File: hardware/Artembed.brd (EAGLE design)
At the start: 79.4 x 31.8 mm, 108 parts, among them J3 CORTEX_JTAG_DEBUG_MINIMUM_PTH, J4 CORTEX_JTAG_DEBUG_PTH_NS, J7 CAMERA-HIMAX, U1 DAPLINK_KL26Z, U2 16MHz, U3 ARTEMIS_MODULESMD, U4 1.8V, U5 LIS2DH12, Y1 32.768kHz

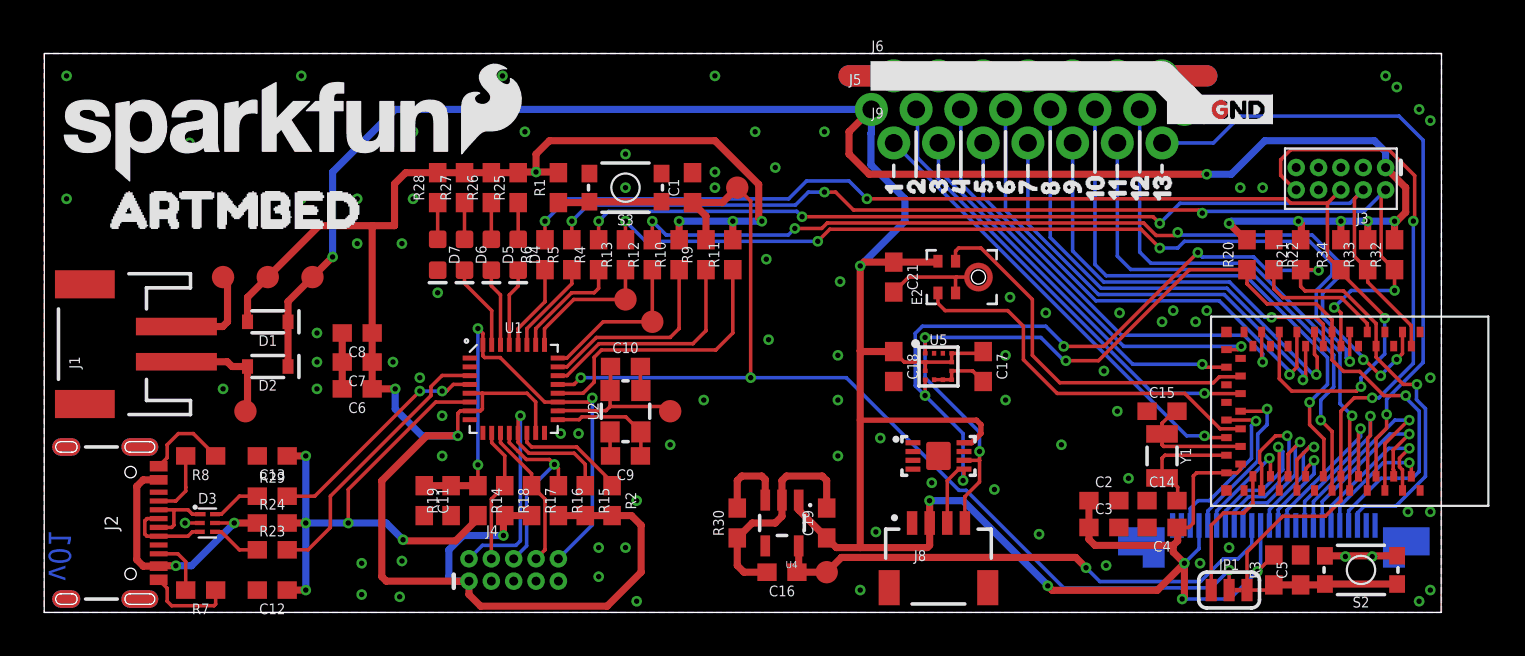
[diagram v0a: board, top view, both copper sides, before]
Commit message: Update XTAL from Eli
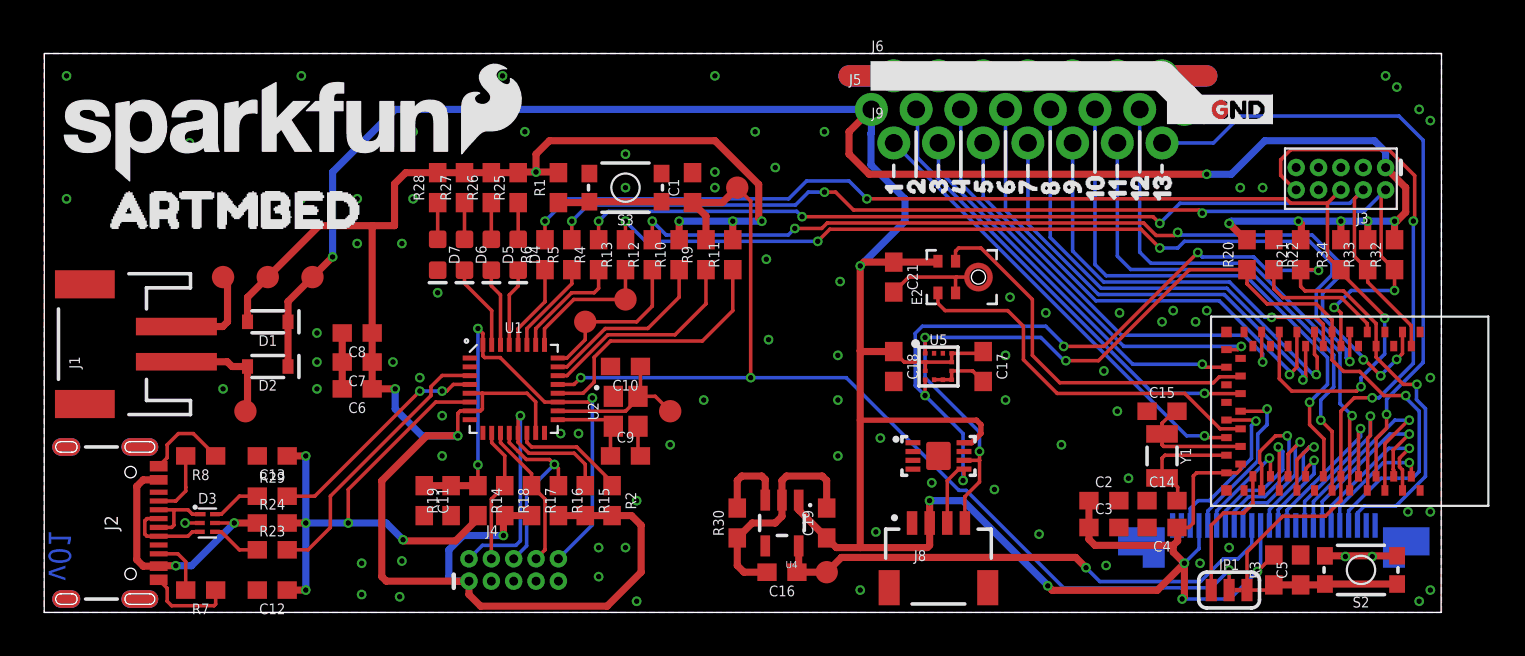
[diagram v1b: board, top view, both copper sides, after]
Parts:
- U2: device SparkFun-Clocks:CRYSTAL-SMD-3.2X2.5MM -> SparkFun-Clocks:CRYSTAL-SMD-2X2.5MM
- moved TP3 3.81 mm to (30.7, 16.5)
- turned C10 to 180 degrees
- turned C9 to 0 degrees
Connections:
- net GND: now also U2.P2, U2.P4; no longer U2.2, U2.4
- net N$13: now also U2.P1; no longer U2.1
- net N$16: now also U2.P3; no longer U2.3
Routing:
- net N$13: track 6.52 -> 5.07 mm
- net N$19: track 11.1 -> 10.1 mm
- net GND: track 83.7 -> 82.7 mm
- net N$22: track 12.9 -> 12.1 mm
- net N$11: track 15.8 -> 15.0 mm

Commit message: proto review revisions, panelized, cammed
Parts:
- added FD1, FD2, FD3, FD4: FIDUCIAL0.2MM, SparkFun-Aesthetics:FIDUCIAL-0.2MM
- added LOGO1: OSHW-LOGOS, SparkFun-Aesthetics:OSHW-LOGO-S
- added U$19: (no value), buzzard_labels_1:COM7
- added U$20: (no value), buzzard_labels_1:HID5
- added U$21: (no value), buzzard_labels_1:MSD6
- added U$22: (no value), buzzard_labels_1:MIC0
- added U$23: (no value), buzzard_labels_1:HW3
- added U$24: (no value), buzzard_labels_1:SW4
- added U$25: (no value), buzzard_labels_1:_RESET_TGT2
- added U$26: (no value), buzzard_labels_1:RESET_IF1
- added U$27: (no value), buzzard_labels_1:3V39
- added U$28: (no value), buzzard_labels_1:VDD8
- LOGO2: value (none) -> SFE_LOGO_NAME.2_INCH
- renumbered U$15 to LOGO2
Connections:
- net CAMERA_DVDD_EN: now also U3.D15
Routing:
- net CAMERA_DVDD_EN: track 4.51 -> 46.1 mm, vias 0 -> 4
